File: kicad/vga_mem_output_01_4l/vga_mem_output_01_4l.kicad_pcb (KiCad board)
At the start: 4 copper layers, 59.4 x 80.8 mm, 37 parts, among them J1 Conn_01x03_Socket, J2 Conn_01x02_Socket, J3 Conn_01x08_Socket, J4 DE15_Socket_HighDensity_Mount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, J5 Conn_01x18_Socket, J6 Conn_01x18_Socket, U1 74LS08, U10 74HCT574, U2 74LS08, U3 UM61512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

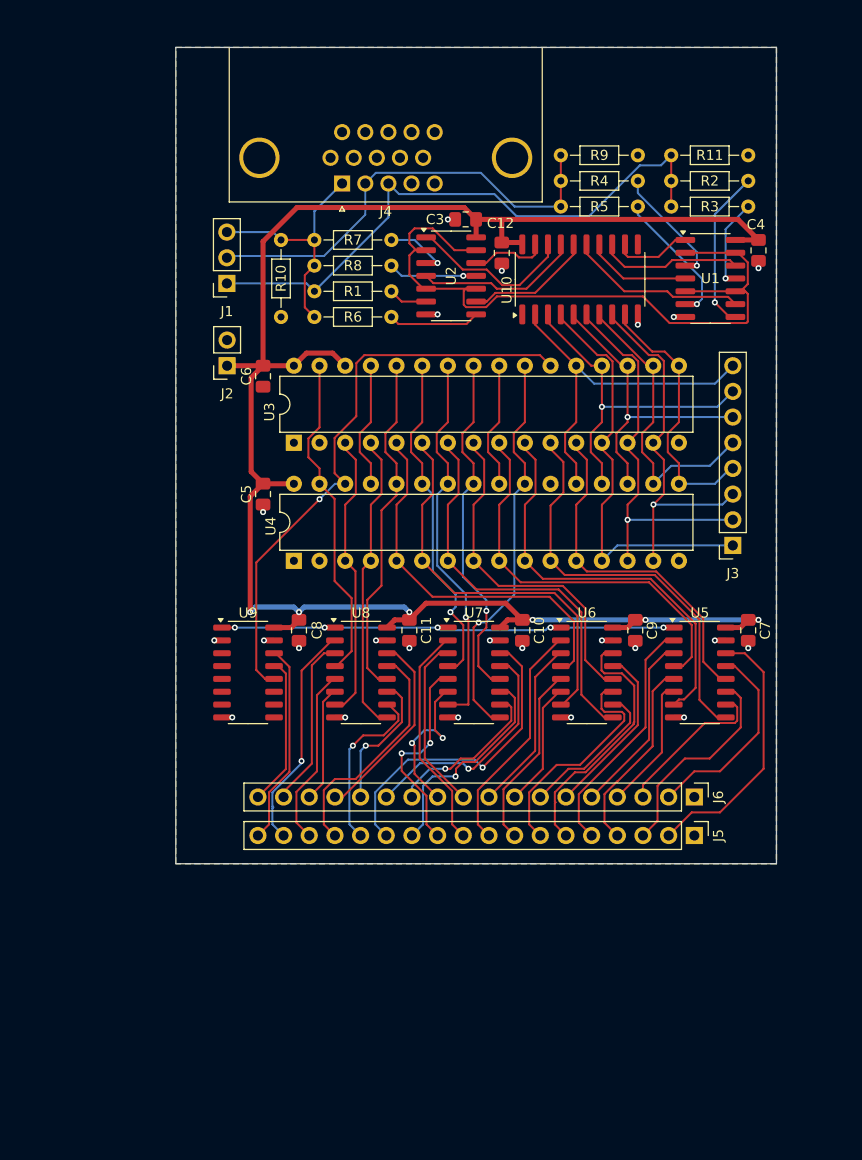
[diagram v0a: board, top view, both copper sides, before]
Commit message: added cpu side bus transceiver
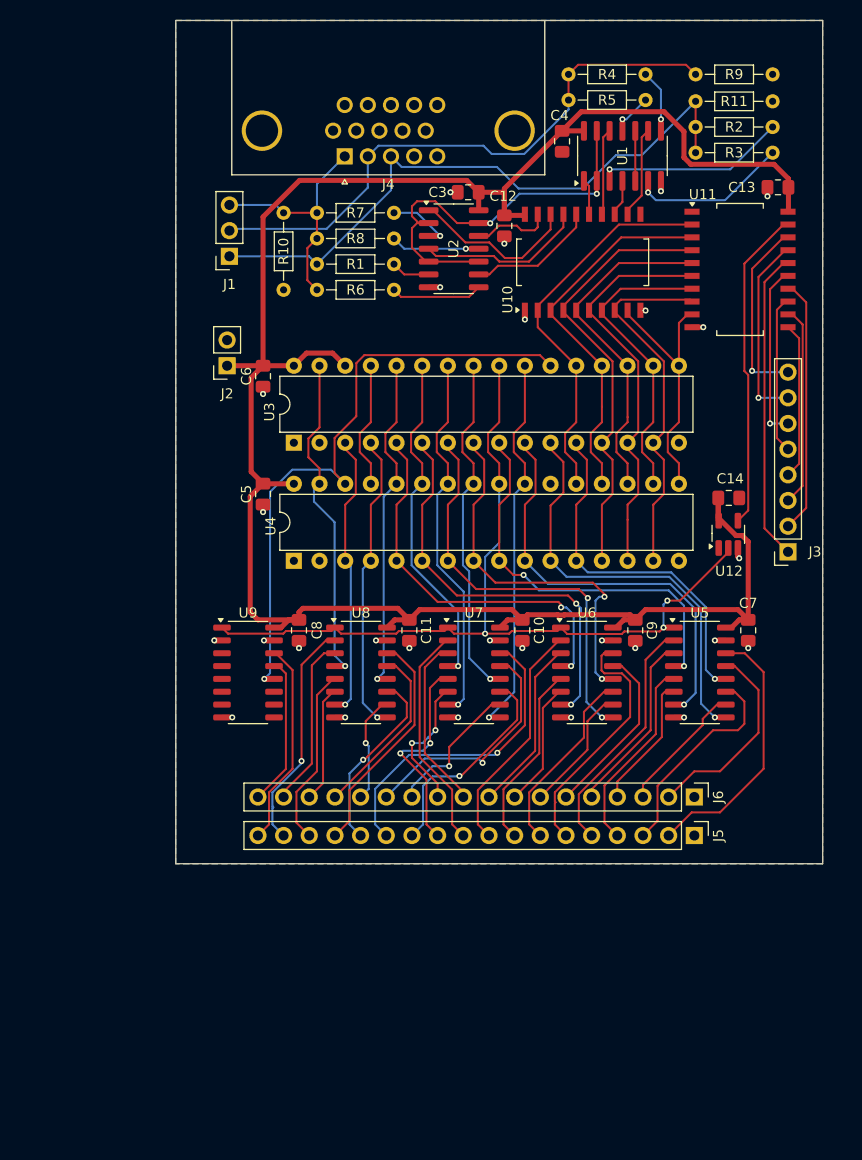
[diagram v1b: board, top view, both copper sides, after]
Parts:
- added C13: 100nF, Capacitor_SMD:C_0805_2012Metric_Pad1.18x1.45mm_HandSolder, F.Cu at (125.1, 53.5)
- added C14: 100nF, Capacitor_SMD:C_0805_2012Metric_Pad1.18x1.45mm_HandSolder, F.Cu at (120.2, 84.2)
- added U11: 74HC245, Package_SO:SO-20_12.8x7.5mm_P1.27mm, F.Cu at (121.4, 61.6)
- added U12: 74AHC1GU04, Package_TO_SOT_SMD:SOT-23-5_HandSoldering, F.Cu at (120.2, 87.8)
- U10: footprint Package_SO:SO-20_5.3x12.6mm_P1.27mm -> Package_SO:SO-20_12.8x7.5mm_P1.27mm
- moved C4 22.2 mm to (103.8, 48.9)
- moved R9 15.6 mm to (124.6, 42.3)
- moved U1 14.9 mm to (109.7, 50.4), turned to 90 degrees
- moved R4 10.6 mm to (112.0, 42.3)
- moved R5 10.6 mm to (112.0, 44.8)
- moved R11 5.85 mm to (124.6, 45.0)
- moved R2 5.85 mm to (124.6, 47.5)
- moved R3 5.85 mm to (124.6, 50.0)
- moved J3 5.50 mm to (126.1, 89.5)
- moved J4 2.70 mm to (82.2, 50.4)
- moved R1 2.70 mm to (87.1, 61.1)
- moved R10 2.70 mm to (76.2, 63.6)
- moved R6 2.70 mm to (87.1, 63.6)
- moved R7 2.70 mm to (87.1, 56.0)
- moved R8 2.70 mm to (87.1, 58.5)
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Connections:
- J3 pad 1: /PD_0 -> /CPU_D0
- J3 pad 2: /PD_1 -> /CPU_D1
- J3 pad 3: /PD_2 -> /CPU_D2
- J3 pad 4: /PD_3 -> /CPU_D3
- J3 pad 5: /PD_4 -> /CPU_D4
- J3 pad 6: /PD_5 -> /CPU_D5
- J3 pad 7: /PD_6 -> /CPU_D6
- J3 pad 8: /PD_7 -> /CPU_D7
- U1 pad 1: /PDB_3 -> /PDB_1
- U1 pad 11: Net-(R3-Pad1) -> Net-(R5-Pad1)
- U1 pad 12: /PDB_2 -> /PDB_4
- U1 pad 3: Net-(R4-Pad1) -> Net-(R2-Pad1)
- U1 pad 4: /PDB_4 -> /PDB_2
- U1 pad 6: Net-(R5-Pad1) -> Net-(R3-Pad1)
- U1 pad 8: Net-(R2-Pad1) -> Net-(R4-Pad1)
- U1 pad 9: /PDB_1 -> /PDB_3
- U3 pad 24: /~{OE} -> /~{A_FRONT}
- U4 pad 24: /~{OE} -> /~{A_FRONT}
- U8 pad 10: /DG_A12 -> /CPU_A12
- U8 pad 11: /CPU_A12 -> /DG_A12
- U8 pad 13: /DG_A13 -> /CPU_A13
- U8 pad 14: /CPU_A13 -> /DG_A13
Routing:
- net /~{A_FRONT}: track 48.0 -> 86.0 mm, vias 5 -> 3
- net /A_FRONT: track 0.00 -> 31.9 mm
- net VCC: track 183.1 -> 214.0 mm, vias 6 -> 0
- net /CPU_D0: track 0.00 -> 30.8 mm
- net /VA_EN: track 73.3 -> 45.7 mm, vias 0 -> 2
- net /CPU_D1: track 0.00 -> 25.3 mm
- net /CPU_D2: track 0.00 -> 19.9 mm
- net /CPU_D6: track 0.00 -> 18.9 mm, vias 0 -> 1
- net /CPU_D7: track 0.00 -> 18.6 mm, vias 0 -> 1
- net /CPU_D5: track 0.00 -> 17.4 mm, vias 0 -> 1
- net /CPU_D4: track 0.00 -> 15.7 mm
- net /CPU_D3: track 0.00 -> 15.5 mm
- net /PDB_1: track 17.7 -> 3.51 mm
- net /G_OUT: track 44.8 -> 57.8 mm
- net /~{OE}: track 12.6 -> 0.00 mm
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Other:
- board size 59.4 x 80.8 mm -> 64 x 83.4 mm

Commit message: 4l vga mem output routing improvements
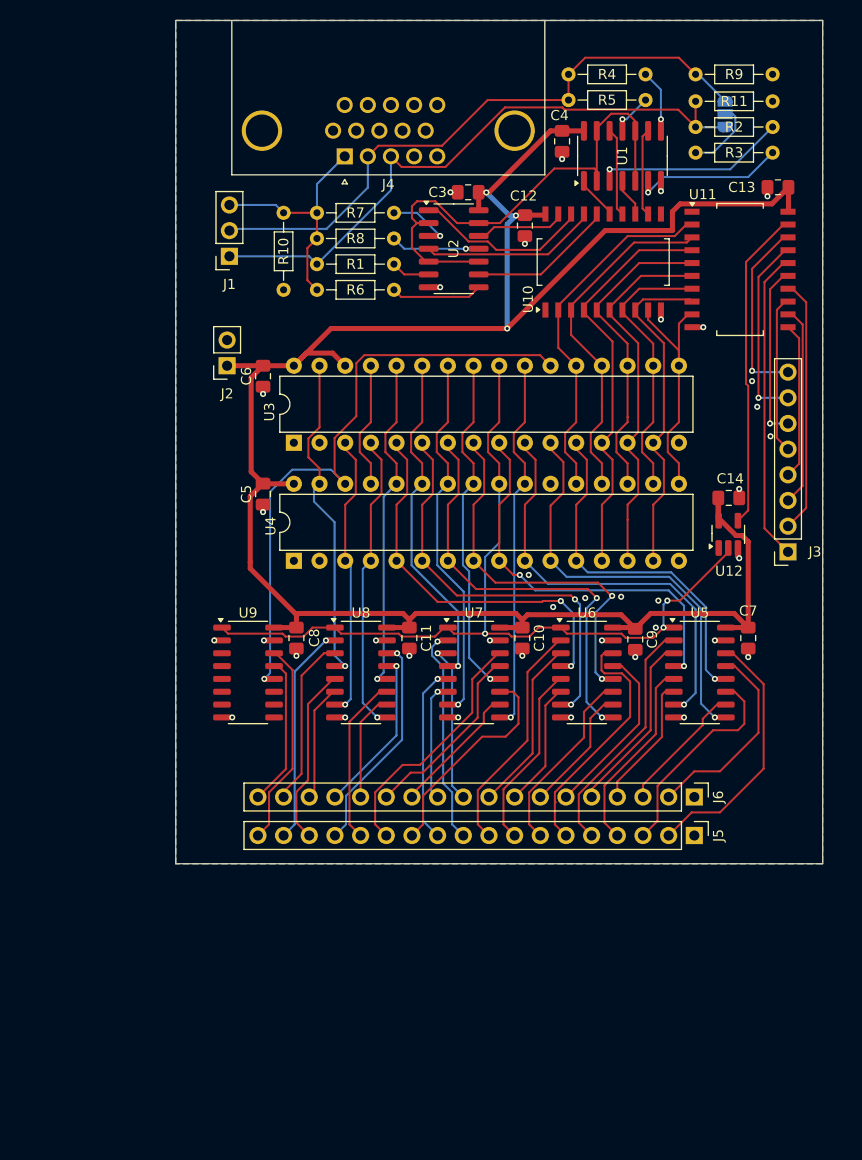
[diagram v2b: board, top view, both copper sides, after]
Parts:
- added JP1: SolderJumper_3_Open, Jumper:SolderJumper-3_P1.3mm_Open_RoundedPad1.0x1.5mm, B.Cu at (119.9, 46.2)
- moved C12 2.03 mm to (100.1, 57.3)
- moved U10 2.03 mm to (107.8, 60.9)
- moved C9 0.89 mm to (111.0, 98.2)
- moved C8 0.80 mm to (77.5, 98.1)
- moved C10 0.76 mm to (99.8, 98.1)
- moved C11 0.76 mm to (88.6, 98.1)
- moved C7 0.76 mm to (122.2, 98.1)
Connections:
- R3 pad 2: /B_OUT -> Net-(JP1-C)
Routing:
- net Net-(JP1-C): track 0.00 -> 7.31 mm
- net /DG_A11: track 31.2 -> 24.7 mm, vias 1 -> 0
- net /VA_EN: track 45.7 -> 51.4 mm, vias 2 -> 0
- net /CPU_A11: track 23.8 -> 18.6 mm, vias 1 -> 0
- net /G_OUT: track 57.8 -> 61.2 mm
- net /DG_A9: track 20.7 -> 17.7 mm, vias 2 -> 1
- net /PD_1: track 40.0 -> 37.0 mm
- net /PD_2: track 36.5 -> 33.6 mm
- net /PD_0: track 43.6 -> 40.7 mm
- net /PD_5: track 33.8 -> 31.0 mm
- net /PD_7: track 38.7 -> 35.8 mm
- net /PD_4: track 30.2 -> 27.4 mm
- net /PD_6: track 37.3 -> 34.6 mm
- net /PDB_5: track 12.6 -> 14.4 mm
- net /CPU_A9: track 13.8 -> 12.0 mm, vias 2 -> 1
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
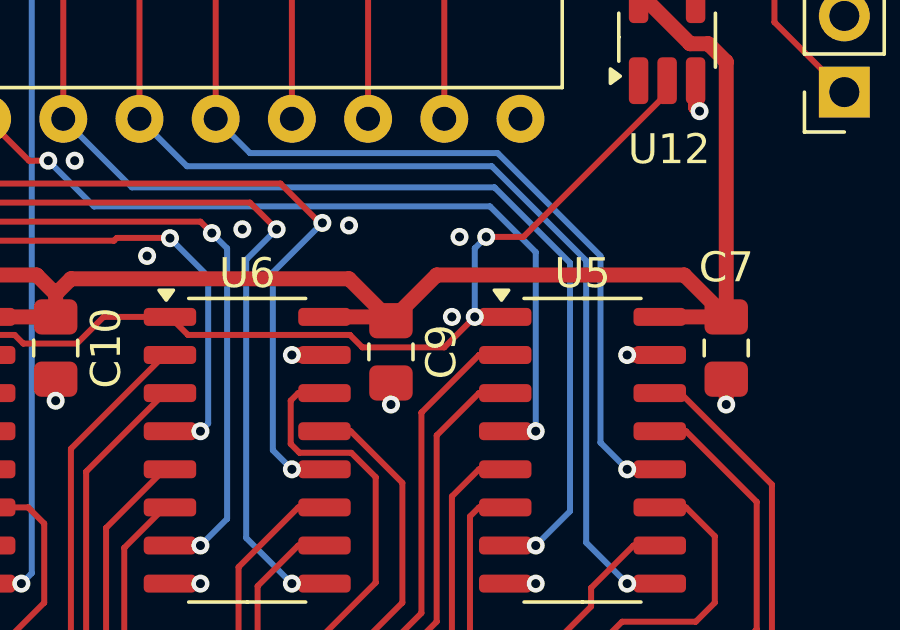
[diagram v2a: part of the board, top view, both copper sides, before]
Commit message: use hierarchical sheet for vga mem output
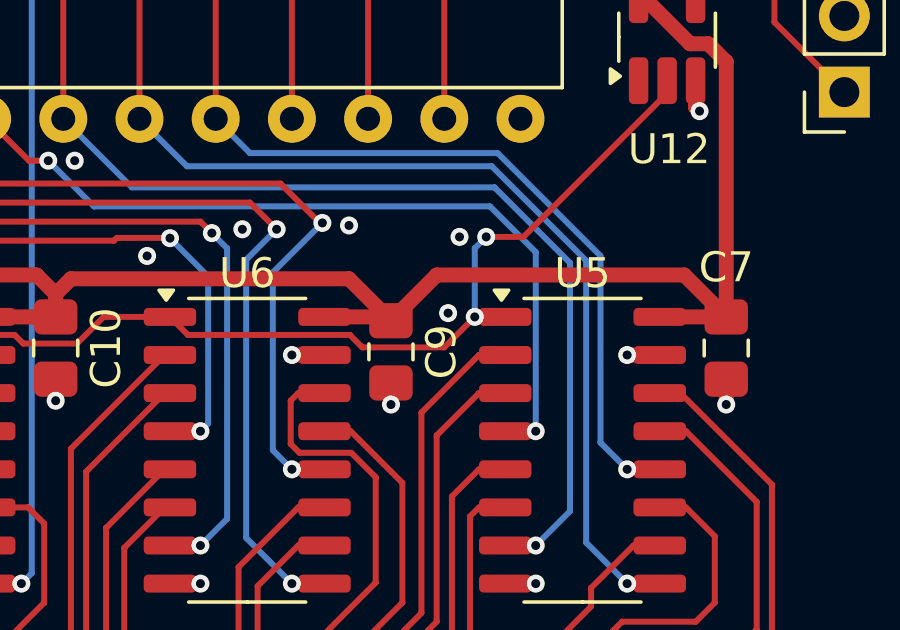
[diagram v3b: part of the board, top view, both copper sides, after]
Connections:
- net /B_OUT renamed /vga output/B_OUT
- net /CPU_A0 renamed /Address multiplexer/CPU_A0
- net /CPU_A1 renamed /Address multiplexer/CPU_A1
- net /CPU_A10 renamed /Address multiplexer/CPU_A10
- net /CPU_A11 renamed /Address multiplexer/CPU_A11
- net /CPU_A12 renamed /Address multiplexer/CPU_A12
- net /CPU_A13 renamed /Address multiplexer/CPU_A13
- net /CPU_A14 renamed /Address multiplexer/CPU_A14
- net /CPU_A15 renamed /Address multiplexer/CPU_A15
- net /CPU_A16 renamed /Address multiplexer/CPU_A16
- net /CPU_A2 renamed /Address multiplexer/CPU_A2
- net /CPU_A3 renamed /Address multiplexer/CPU_A3
- net /CPU_A4 renamed /Address multiplexer/CPU_A4
- net /CPU_A5 renamed /Address multiplexer/CPU_A5
- net /CPU_A6 renamed /Address multiplexer/CPU_A6
- net /CPU_A7 renamed /Address multiplexer/CPU_A7
- net /CPU_A8 renamed /Address multiplexer/CPU_A8
- net /CPU_A9 renamed /Address multiplexer/CPU_A9
- net /DG_A0 renamed /Address multiplexer/DG_A0
- net /DG_A1 renamed /Address multiplexer/DG_A1
- net /DG_A10 renamed /Address multiplexer/DG_A10
- net /DG_A11 renamed /Address multiplexer/DG_A11
- net /DG_A12 renamed /Address multiplexer/DG_A12
- net /DG_A13 renamed /Address multiplexer/DG_A13
- net /DG_A14 renamed /Address multiplexer/DG_A14
- net /DG_A15 renamed /Address multiplexer/DG_A15
- net /DG_A16 renamed /Address multiplexer/DG_A16
- net /DG_A2 renamed /Address multiplexer/DG_A2
- net /DG_A3 renamed /Address multiplexer/DG_A3
- net /DG_A4 renamed /Address multiplexer/DG_A4
- net /DG_A5 renamed /Address multiplexer/DG_A5
- net /DG_A6 renamed /Address multiplexer/DG_A6
- net /DG_A7 renamed /Address multiplexer/DG_A7
- net /DG_A8 renamed /Address multiplexer/DG_A8
- net /DG_A9 renamed /Address multiplexer/DG_A9
- net /G_OUT renamed /vga output/G_OUT
- net /R_OUT renamed /vga output/R_OUT
- net /VA_EN renamed /vga output/VA_EN

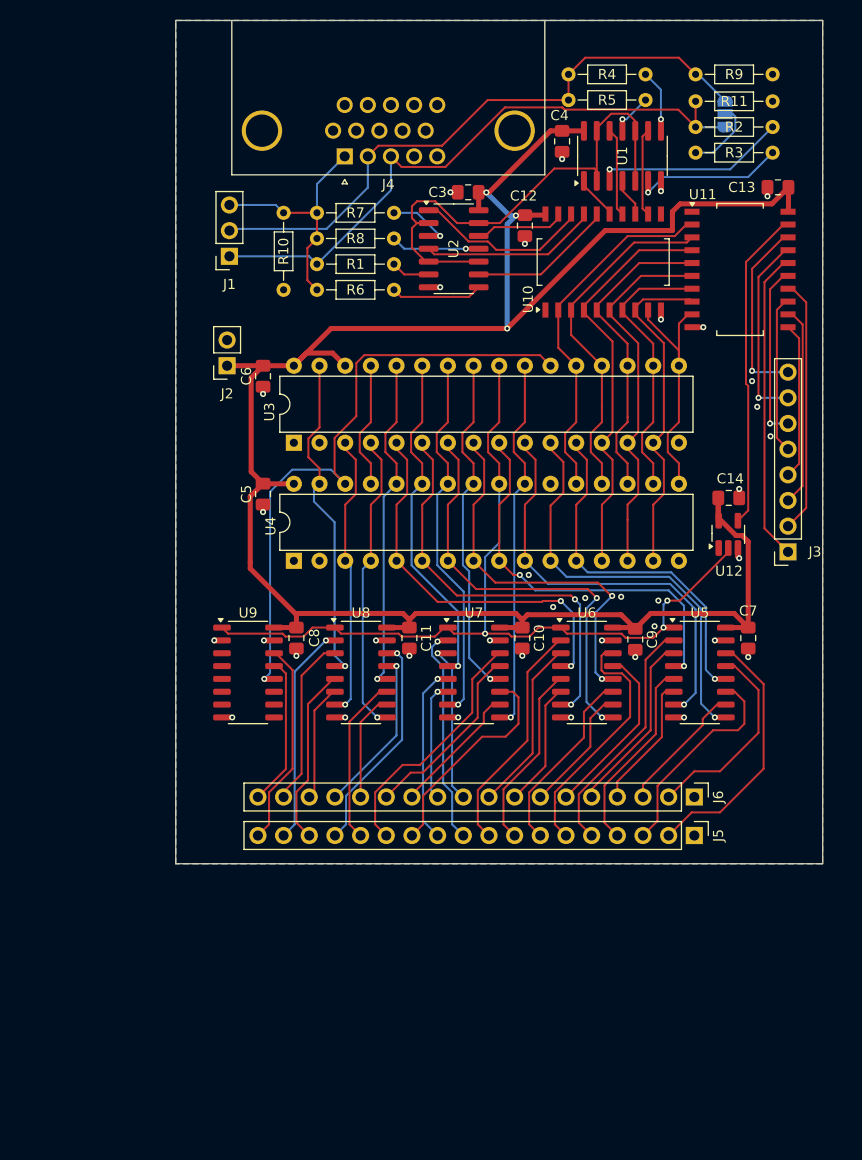
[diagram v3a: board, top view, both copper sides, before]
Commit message: added clock circuit ('display generator')
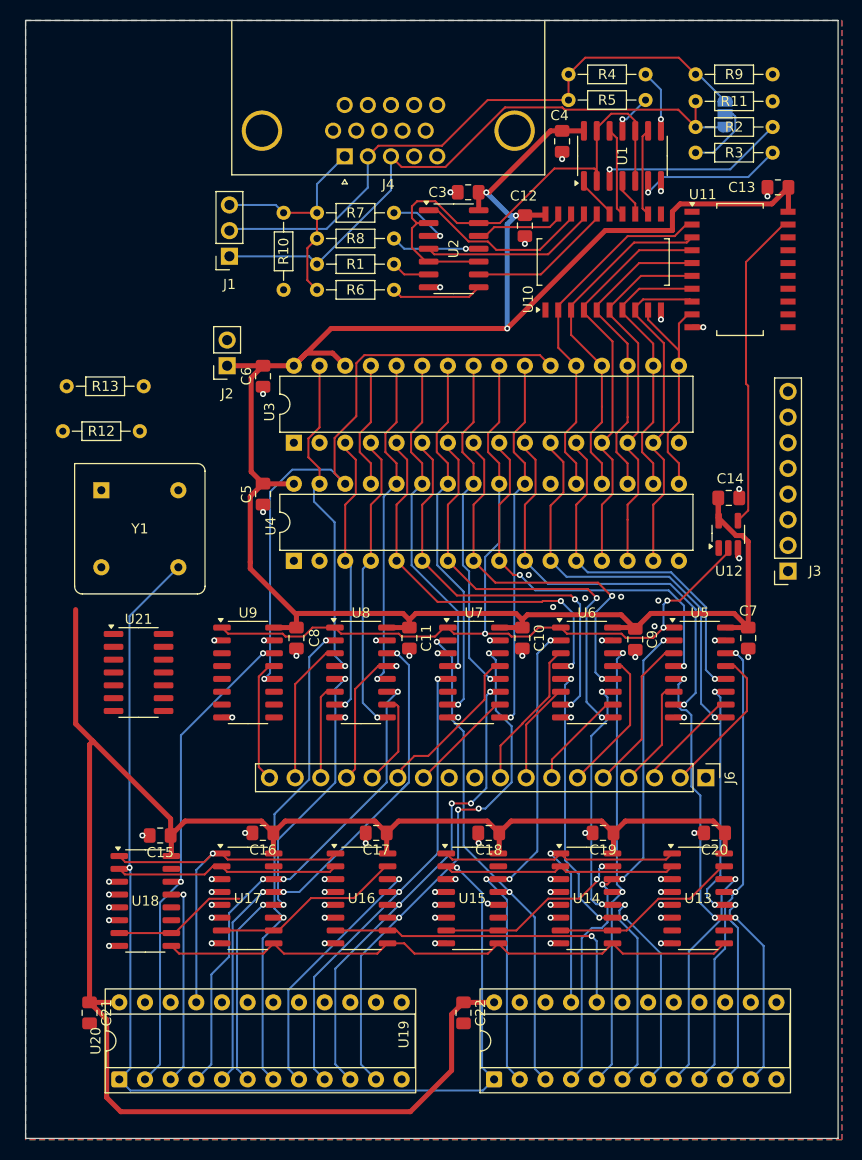
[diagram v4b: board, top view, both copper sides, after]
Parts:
- removed J5: Conn_01x18_Socket, Connector_PinHeader_2.54mm:PinHeader_1x18_P2.54mm_Vertical
- added C15: 100nF, Capacitor_SMD:C_0805_2012Metric_Pad1.18x1.45mm_HandSolder, F.Cu at (64.0, 117.6)
- added C16: 100nF, Capacitor_SMD:C_0805_2012Metric_Pad1.18x1.45mm_HandSolder, F.Cu at (74.2, 117.3)
- added C17: 100nF, Capacitor_SMD:C_0805_2012Metric_Pad1.18x1.45mm_HandSolder, F.Cu at (85.4, 117.3)
- added C18: 100nF, Capacitor_SMD:C_0805_2012Metric_Pad1.18x1.45mm_HandSolder, F.Cu at (96.5, 117.3)
- added C19: 100nF, Capacitor_SMD:C_0805_2012Metric_Pad1.18x1.45mm_HandSolder, F.Cu at (107.8, 117.3)
- added C20: 100nF, Capacitor_SMD:C_0805_2012Metric_Pad1.18x1.45mm_HandSolder, F.Cu at (118.9, 117.3)
- added C21: 100nF, Capacitor_SMD:C_0805_2012Metric_Pad1.18x1.45mm_HandSolder, F.Cu at (57.0, 135.1)
- added C22: 100nF, Capacitor_SMD:C_0805_2012Metric_Pad1.18x1.45mm_HandSolder, F.Cu at (94.0, 135.1)
- added R12: R, Resistor_THT:R_Axial_DIN0204_L3.6mm_D1.6mm_P7.62mm_Horizontal, F.Cu at (54.4, 77.6)
- added R13: R, Resistor_THT:R_Axial_DIN0204_L3.6mm_D1.6mm_P7.62mm_Horizontal, F.Cu at (54.7, 73.2)
- added U13: 74LS163, Package_SO:SO-16_3.9x9.9mm_P1.27mm, F.Cu at (117.2, 123.8)
- added U14: 74LS163, Package_SO:SO-16_3.9x9.9mm_P1.27mm, F.Cu at (106.2, 123.8)
- added U15: 74LS163, Package_SO:SO-16_3.9x9.9mm_P1.27mm, F.Cu at (94.9, 123.8)
- added U16: 74LS163, Package_SO:SO-16_3.9x9.9mm_P1.27mm, F.Cu at (83.9, 123.8)
- added U17: 74LS163, Package_SO:SO-16_3.9x9.9mm_P1.27mm, F.Cu at (72.6, 123.8)
- added U18: 74LS163, Package_SO:SO-16_3.9x9.9mm_P1.27mm, F.Cu at (62.5, 124.1)
- added U19: PAL20RS10, Package_DIP:DIP-24_W7.62mm_Socket, F.Cu at (97.0, 141.7)
- added U20: PAL20RS10, Package_DIP:DIP-24_W7.62mm_Socket, F.Cu at (59.9, 141.7)
- added U21: 74LS08, Package_SO:SO-14_3.9x8.65mm_P1.27mm, F.Cu at (61.8, 101.5)
- added Y1: CXO_DIP8, Oscillator:Oscillator_DIP-8, F.Cu at (58.2, 83.4)
- moved J6 2.22 mm to (118.0, 111.9)
- moved J3 1.91 mm to (126.1, 91.4)
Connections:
- net /vga output/VA_EN renamed /display_generator/VA_EN
- J4 pad 13: unconnected-(J4-Pad13) -> Net-(J4-Pad13)
- J4 pad 14: unconnected-(J4-Pad14) -> Net-(J4-Pad14)
- J4 pad 5: unconnected-(J4-Pad5) -> GND
- U5 pad 11: /Address multiplexer/DG_A1 -> /display_generator/H2
- U5 pad 14: /Address multiplexer/DG_A0 -> /display_generator/H1
- U5 pad 2: /Address multiplexer/DG_A3 -> /display_generator/H4
- U5 pad 5: /Address multiplexer/DG_A2 -> /display_generator/H3
- U6 pad 11: /Address multiplexer/DG_A5 -> /display_generator/H6
- U6 pad 14: /Address multiplexer/DG_A4 -> /display_generator/H5
- U6 pad 2: /Address multiplexer/DG_A7 -> /display_generator/H8
- U6 pad 5: /Address multiplexer/DG_A6 -> /display_generator/H7
- U7 pad 11: /Address multiplexer/DG_A10 -> /display_generator/V2
- U7 pad 14: /Address multiplexer/DG_A11 -> /display_generator/V3
- U7 pad 2: /Address multiplexer/DG_A8 -> /display_generator/H9
- U7 pad 5: /Address multiplexer/DG_A9 -> /display_generator/V1
- U8 pad 11: /Address multiplexer/DG_A12 -> /display_generator/V4
- U8 pad 14: /Address multiplexer/DG_A13 -> /display_generator/V5
- U8 pad 2: /Address multiplexer/DG_A15 -> /display_generator/V7
- U8 pad 5: /Address multiplexer/DG_A14 -> /display_generator/V6
- U9 pad 14: /Address multiplexer/DG_A16 -> /display_generator/V8
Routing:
- net VCC: track 214.3 -> 457.2 mm
- net /display_generator/CLOCK: track 0.00 -> 161.5 mm, vias 0 -> 2
- net /display_generator/V5: track 0.00 -> 54.3 mm, vias 0 -> 3
- net /display_generator/V3: track 0.00 -> 53.7 mm, vias 0 -> 4
- net /display_generator/H4: track 0.00 -> 50.1 mm, vias 0 -> 3
- net /display_generator/H9: track 0.00 -> 50.0 mm, vias 0 -> 2
- net /display_generator/H8: track 0.00 -> 49.8 mm, vias 0 -> 3
- net /display_generator/V4: track 0.00 -> 49.2 mm, vias 0 -> 3
- net /display_generator/V7: track 0.00 -> 49.1 mm, vias 0 -> 2
- net /display_generator/V8: track 0.00 -> 49.0 mm, vias 0 -> 2
- net /display_generator/V2: track 0.00 -> 48.5 mm, vias 0 -> 4
- net /display_generator/V1: track 0.00 -> 47.3 mm, vias 0 -> 2
- net /display_generator/V6: track 0.00 -> 47.2 mm, vias 0 -> 3
- net /display_generator/H7: track 0.00 -> 46.8 mm, vias 0 -> 3
- net /display_generator/H3: track 0.00 -> 46.3 mm, vias 0 -> 3
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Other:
- board size 64 x 83.4 mm -> 80.4 x 110.6 mm
